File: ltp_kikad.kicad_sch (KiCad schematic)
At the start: 7 parts, among them J2 RPi_GPIO

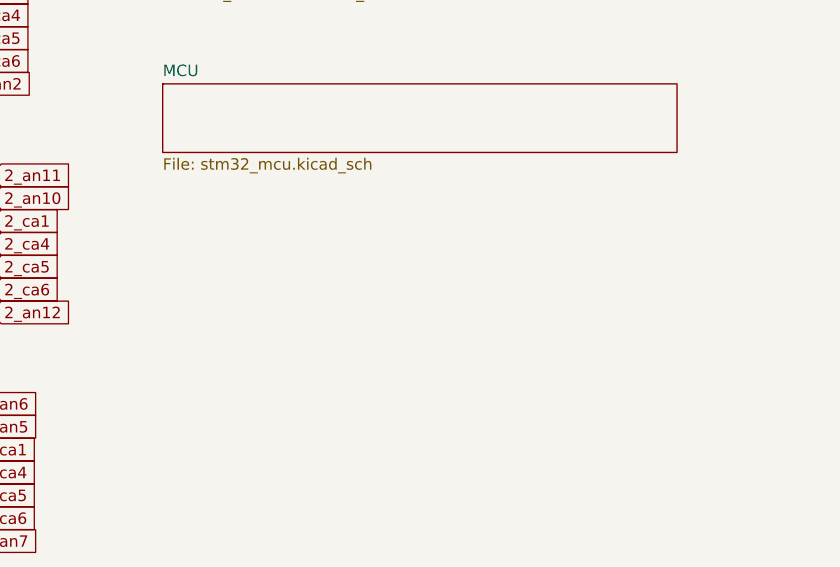
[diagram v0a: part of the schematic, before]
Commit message: Add dc-dc 3.3v to 5v
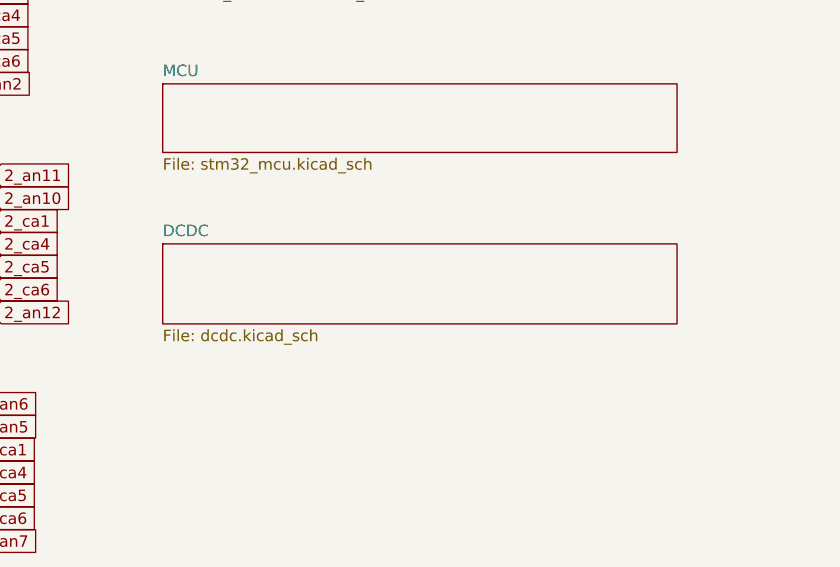
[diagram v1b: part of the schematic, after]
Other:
- added sheet DCDC (dcdc.kicad_sch)
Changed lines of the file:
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@@
+    )
+  )
+  (sheet (at 116.84 125.73) (size 57.15 8.89) (fields_autoplaced)
+    (stroke (width 0.1524) (type solid))
+    (fill (color 0 0 0 0.0000))
+    (property "Sheetname" "DCDC" (at 116.84 125.0184 0)
+      (effects (font (size 1.27 1.27)) (justify left bottom))
+    )
+    (property "Sheetfile" "dcdc.kicad_sch" (at 116.84 135.2046 0)
+      (effects (font (size 1.27 1.27)) (justify left top))
+    )
+    (property "Field2" "" (at 116.84 125.73 0)
+      (effects (font (size 1.27 1.27)) hide)
+    )
+    (instances
+      (project "ltp_kikad"
+        (path "/eed35b77-cbf9-4596-9b17-2558f81058ba" (page "5"))
+      )
     )
   )

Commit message: Add i2c transciever, Pitanga V2
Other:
- added sheet I2c_tranciever (i2c_tramsciever.kicad_sch)
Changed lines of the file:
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@@
+    )
+  )
+  (sheet (at 116.84 41.91) (size 57.15 8.89) (fields_autoplaced)
+    (stroke (width 0.1524) (type solid))
+    (fill (color 0 0 0 0.0000))
+    (property "Sheetname" "I2c_tranciever" (at 116.84 41.1984 0)
+      (effects (font (size 1.27 1.27)) (justify left bottom))
+    )
+    (property "Sheetfile" "i2c_tramsciever.kicad_sch" (at 116.84 51.3846 0)
+      (effects (font (size 1.27 1.27)) (justify left top))
+    )
+    (instances
+      (project "ltp_kikad"
+        (path "/eed35b77-cbf9-4596-9b17-2558f81058ba" (page "6"))
+      )
     )
   )

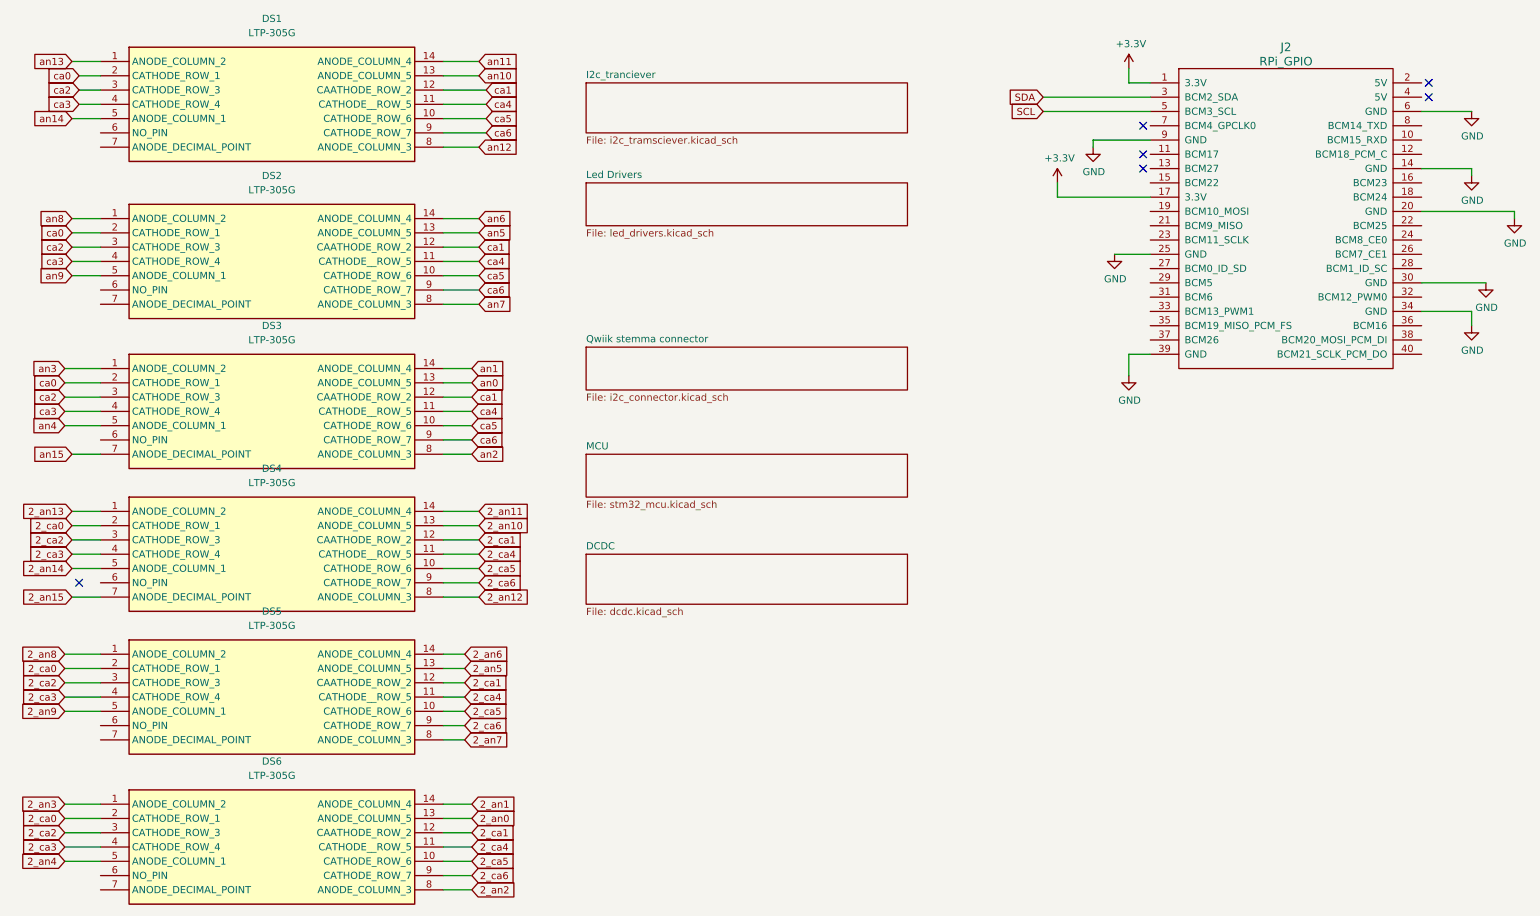
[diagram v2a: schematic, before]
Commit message: Add title block
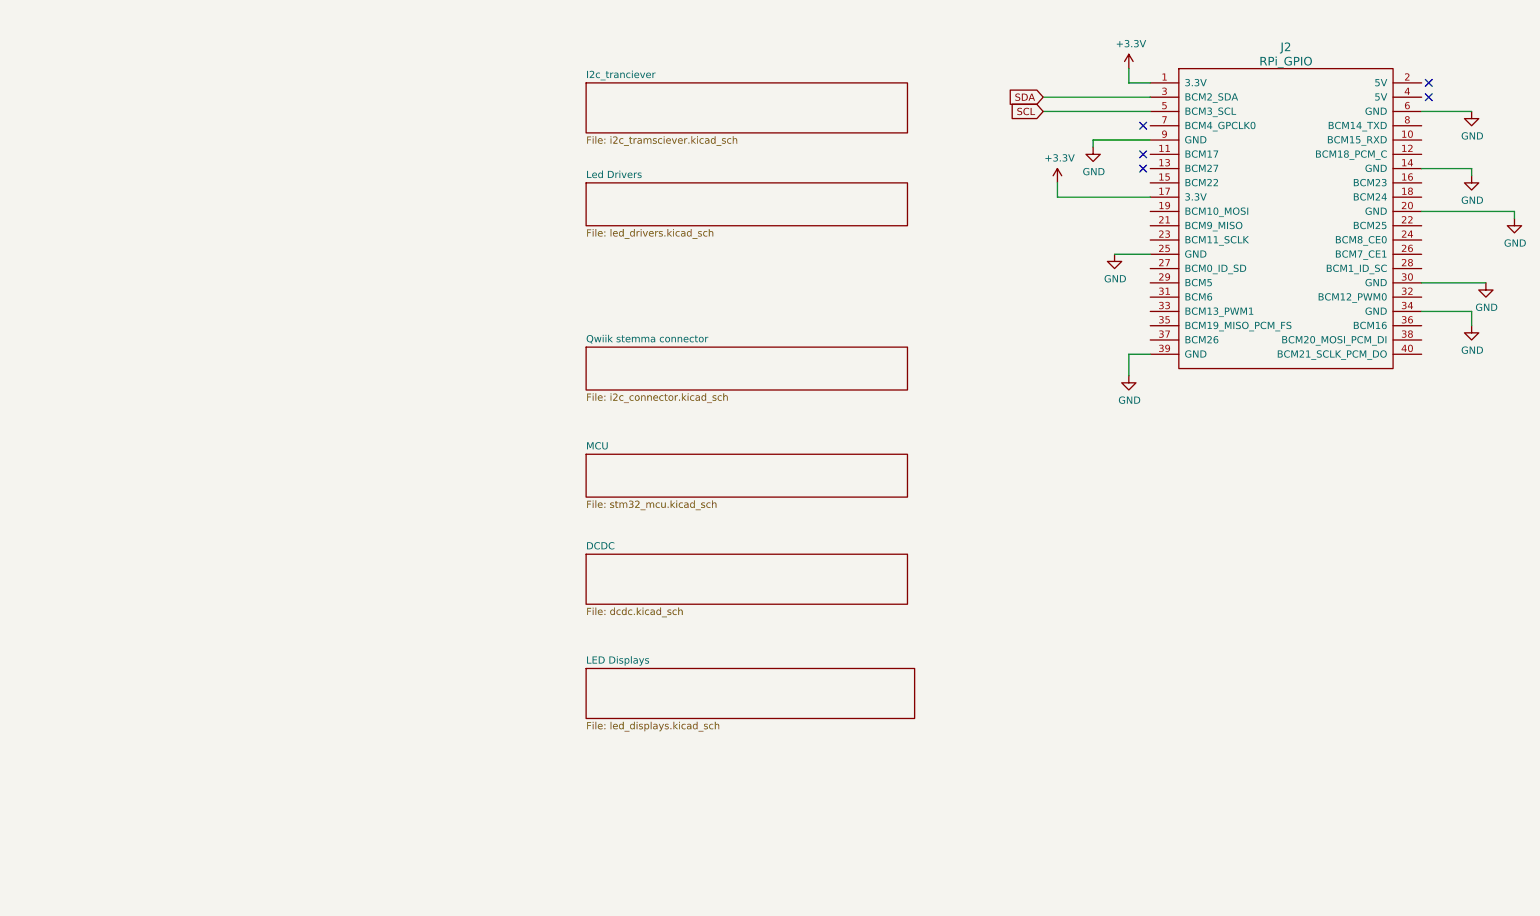
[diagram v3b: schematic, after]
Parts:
- removed DS1, DS2, DS3, DS4, DS5, DS6: LTP-305G, LTP-305G:DIPS762W50P254L1850H400Q14N, symbol LTP-305G:LTP-305G
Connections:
- no-connect marks 6 -> 5
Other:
- added sheet LED Displays (led_displays.kicad_sch)
- company: (none) -> Andrew Tudoroi
- title: (none) -> Pitanga HAT
